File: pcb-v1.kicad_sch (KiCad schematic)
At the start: 32 parts, among them J1 Conn_01x03_Socket, J10 Screw_Terminal_01x04, J11 Screw_Terminal_01x04, J12 Screw_Terminal_01x04, J13 Screw_Terminal_01x04, J14 Screw_Terminal_01x06, J15 Conn_01x06_Pin, J2 Conn_01x03_Socket, J3 Conn_01x03_Socket, J4 Conn_01x03_Socket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

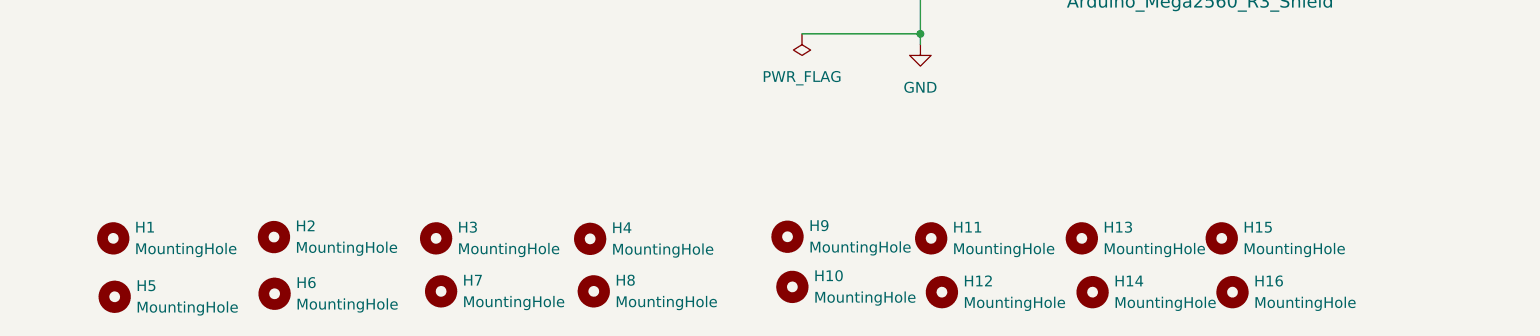
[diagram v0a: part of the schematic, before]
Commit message: adjust foot print to small size
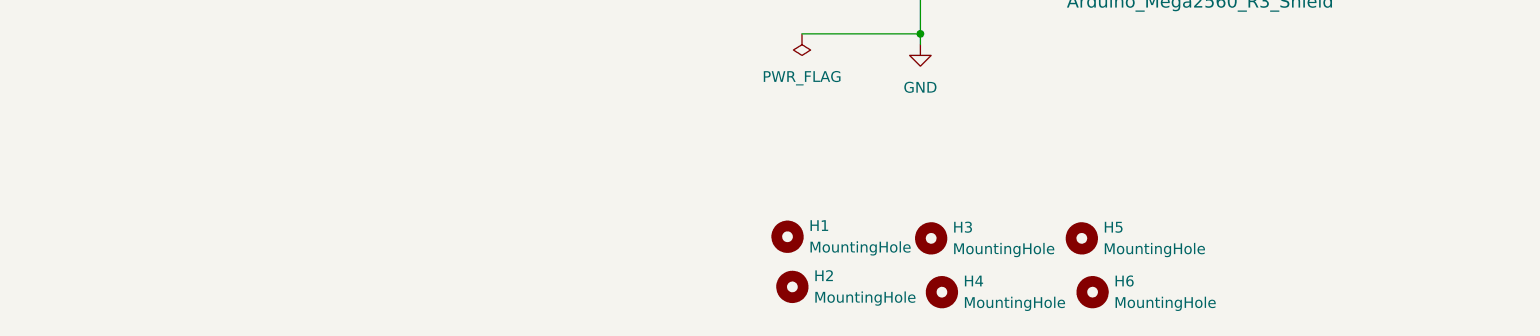
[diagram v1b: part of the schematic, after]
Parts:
- removed H1, H2, H3, H4, H5, H6, H7, H8: MountingHole, MountingHole:MountingHole_3.2mm_M3, symbol Mechanical:MountingHole
- removed H15, H16: MountingHole, MountingHole:MountingHole_4.5mm, symbol Mechanical:MountingHole
- J10, J11, J12, J13: footprint TerminalBlock_Phoenix:TerminalBlock_Phoenix_MKDS-3-4-5.08_1x04_P5.08mm_Horizontal -> TerminalBlock-bornier:TerminalBlock_bornier-4_P5.08mm
- J14: footprint TerminalBlock_Phoenix:TerminalBlock_Phoenix_MKDS-3-6-5.08_1x06_P5.08mm_Horizontal -> TerminalBlock-bornier:TerminalBlock_bornier-6_P5.08mm
- J15, J9: footprint Connector_Molex:Molex_KK-396_A-41792-0006_1x06_P3.96mm_Horizontal -> Connector_Molex:Molex_SPOX_5267-06A_1x06_P2.50mm_Vertical
- renumbered H9 to H1, H10 to H2, H11 to H3, H12 to H4, H13 to H5, H14 to H6

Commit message: finish pcb
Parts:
- J1: for equipment? Voltage Sensor -> Belt
- J10: for equipment? Power 7-8V From Step Down -> Power 8V From Step Down
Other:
- note added: "8V"
- note removed: "7-8V"
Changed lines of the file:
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@@
 		)
 	)
-	(text "7-8V"
+	(text "8V"
 		(exclude_from_sim no)
 		(at 227.838 85.09 0)
@@
 		(property "Value" "MountingHole"
 			(at 127 186.6899 0)
+			(hide yes)
 			(show_name no)
 			(do_not_autoplace no)
@@
 		(property "Value" "MountingHole"
 			(at 144.78 186.6899 0)
+			(hide yes)
 			(show_name no)
 			(do_not_autoplace no)
@@
 			)
 		)
-		(property "for equipment?" "Power 7-8V From Step Down"
+		(property "for equipment?" "Power 8V From Step Down"
 			(at 249.428 87.63 0)
 			(show_name no)
@@
 		(property "Value" "MountingHole"
 			(at 128.27 193.0399 0)
+			(hide yes)
 			(show_name no)
 			(do_not_autoplace no)
@@
 		(property "Value" "MountingHole"
 			(at 146.05 193.0399 0)
+			(hide yes)
 			(show_name no)
 			(do_not_autoplace no)
@@
 		(property "Value" "MountingHole"
 			(at 110.048 186.4989 0)
+			(hide yes)
 			(show_name no)
 			(do_not_autoplace no)
@@
 		(property "Value" "MountingHole"
 			(at 110.6208 192.4183 0)
+			(hide yes)
 			(show_name no)
 			(do_not_autoplace no)
@@
 			)
 		)
-		(property "for equipment?" "Voltage Sensor"
+		(property "for equipment?" "Belt"
 			(at 63.881 43.307 0)
 			(show_name no)
